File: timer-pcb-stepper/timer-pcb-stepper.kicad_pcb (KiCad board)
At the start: 4 copper layers, 75 x 72.5 mm, 30 parts, among them J1 JST_05, J10 JST_05, J11 Conn_01x04_Pin, J2 battery, J3 On/off, J4 JST_03, J5 JST_03, J6 JST_03, J7 JST_03, J8 JST_03_Led_panel, J9 JST_05, U2 ULN2003, U3 ULN2003, U4 ULN2003

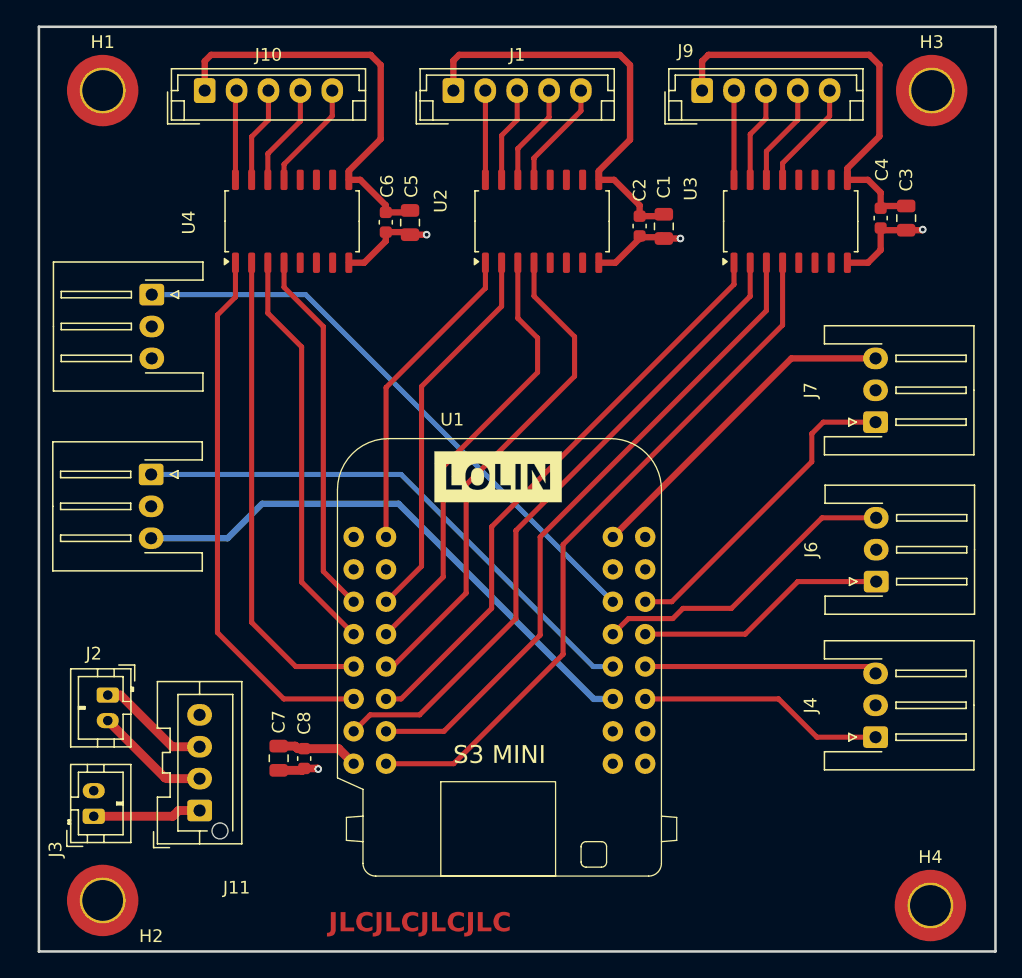
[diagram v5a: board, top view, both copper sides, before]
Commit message: ajout de text indicatif couche silkscreen sur les différents composants du PCB. ajout de test points sur 5V, GND, GPIO37 pour debugger et pin 15 (3.3V). connecteurs repositionés franc bord.
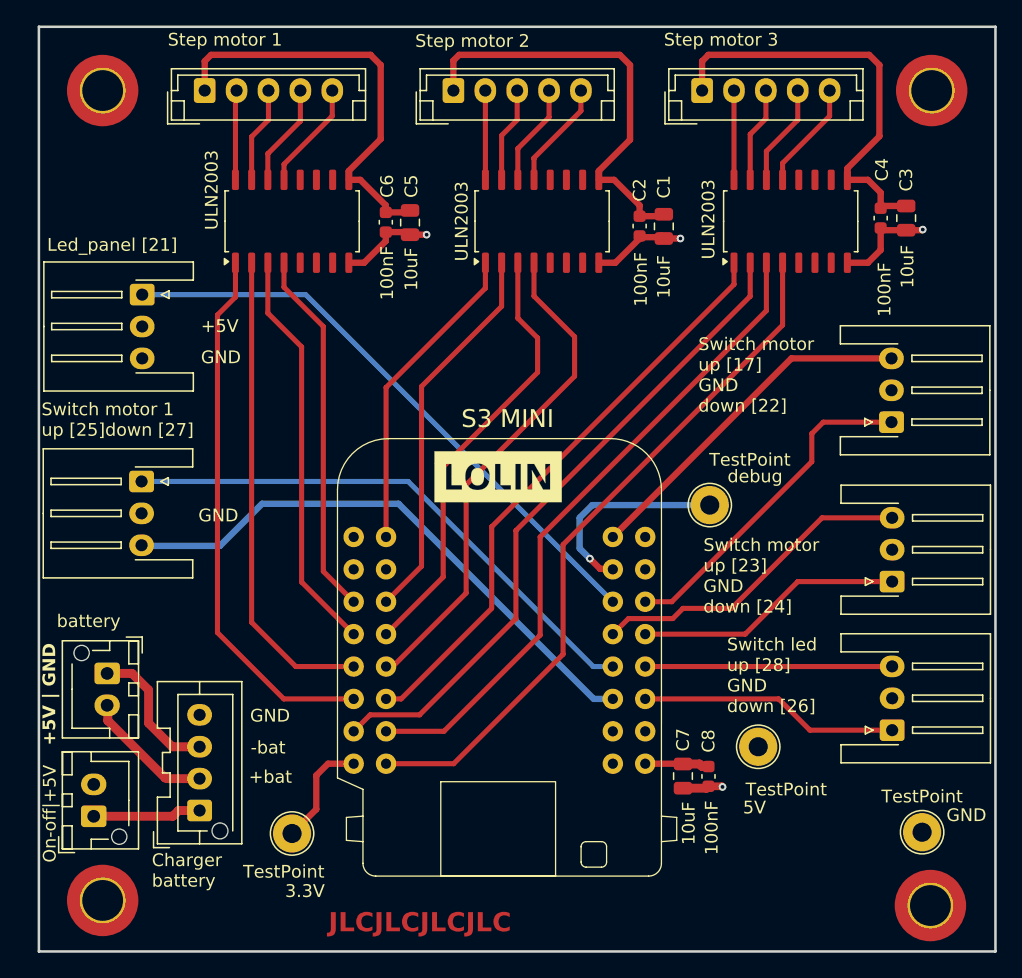
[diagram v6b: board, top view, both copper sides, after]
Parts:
- added TP1: TestPoint, TestPoint:TestPoint_Loop_D2.54mm_Drill1.5mm_Beaded, F.Cu at (69.8, 103.2)
- added TP2: TestPoint, TestPoint:TestPoint_Loop_D2.54mm_Drill1.5mm_Beaded, F.Cu at (106.4, 96.5)
- added TP3: TestPoint, TestPoint:TestPoint_Loop_D2.54mm_Drill1.5mm_Beaded, F.Cu at (102.6, 77.5)
- added TP4: TestPoint, TestPoint:TestPoint_Loop_D2.54mm_Drill1.5mm_Beaded, F.Cu at (119.2, 103.2)
- J2: footprint Connector_JST:JST_PH_B2B-PH-K_1x02_P2.00mm_Vertical -> Connector_JST:JST_XH_B2B-XH-AM_1x02_P2.50mm_Vertical
- J3: value On/off -> On-off|+5V; footprint Connector_JST:JST_PH_B2B-PH-K_1x02_P2.00mm_Vertical -> Connector_JST:JST_XH_B2B-XH-AM_1x02_P2.50mm_Vertical
- J8: value JST_03_Led_panel -> Led_panel [21]
- moved C7 31.7 mm to (100.5, 98.8)
- moved C8 31.7 mm to (102.5, 98.8)
- moved J2 1.70 mm to (55.4, 90.7)
- moved J4 1.41 mm to (116.9, 95.2)
- moved J6 1.25 mm to (116.9, 83.5)
- moved J7 1.25 mm to (116.8, 71.0)
- moved J5 0.93 mm to (58.0, 75.7)
- moved J8 0.75 mm to (58.1, 61.0)
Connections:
- U1 pad 15: +5V -> Net-(U1-3V)
- U1 pad 19: unconnected-(U1-GPIO37-Pad19) -> Net-(U1-GPIO37)
- U1 pad 32: unconnected-(U1-VBUS-Pad32) -> +5V
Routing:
- net Net-(U1-GPIO37): track 0.00 -> 16.3 mm, vias 0 -> 1
- net Net-(U1-3V): track 0.00 -> 8.65 mm
- net -BATT: track 8.88 -> 11.2 mm
- net Switch_Led_control_Up: track 19.3 -> 21.2 mm
- net +5V: track 106.0 -> 104.6 mm
- net Switch_motor_3_Down: track 25.2 -> 26.4 mm
- net Switch_motor_2_Up: track 24.4 -> 25.7 mm
- net Switch_motor_2_Down: track 19.8 -> 21.1 mm
- net +BATT: track 9.08 -> 10.3 mm
- net Switch_Led_control_Down: track 18.3 -> 19.4 mm
- net Switch_motor_1_Down: track 43.7 -> 44.7 mm
- net Switch_motor_3_Up: track 26.6 -> 27.6 mm
- net WS2812_Led: track 46.1 -> 46.9 mm
- net Switch_motor_1_Up: track 42.4 -> 43.0 mm
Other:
- board text added: "+5V"
- board text added: "+5V | GND"
- board text added: "+bat"
- board text added: "-bat"
- board text added: "3.3V"
- board text added: "5V"
- board text added: "Charger battery"
- board text added: "GND"
- board text added: "Step motor 1"
- board text added: "Step motor 2"
- board text added: "Step motor 3"
- board text added: "Switch led up [28] GND down [26]"
- board text added: "Switch motor 1 up [25]down [27]"
- board text added: "Switch motor up [17] GND down [22]"
- board text added: "Switch motor up [23] GND down [24]"
- board text added: "debug"

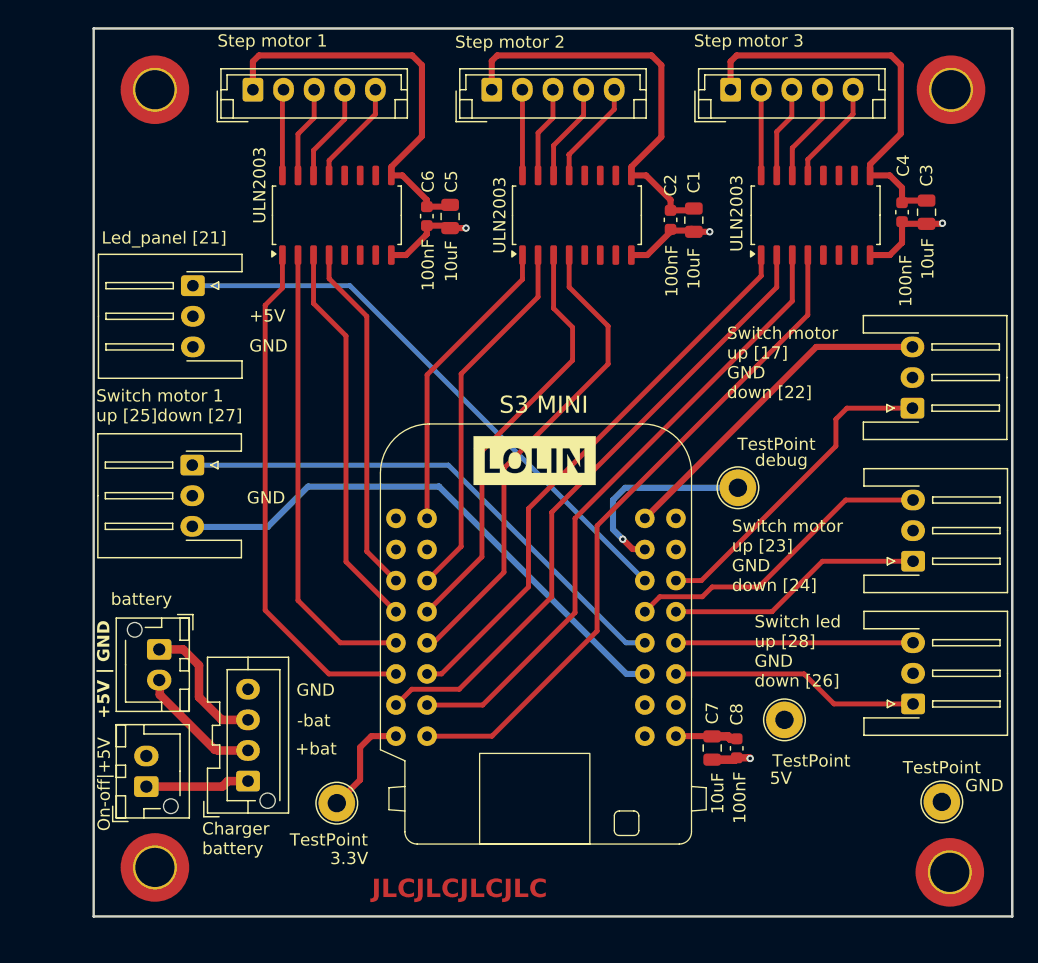
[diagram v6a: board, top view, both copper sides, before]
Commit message: mise à jour fichier blender pour impression 3D. Reste a mettre la bonne épaisseur pour le socle de la shell et percer les trous pour interrupteurs switch et on-off. déterminer ou placer entrées pour recharge et update code. comment fixer module recharge.
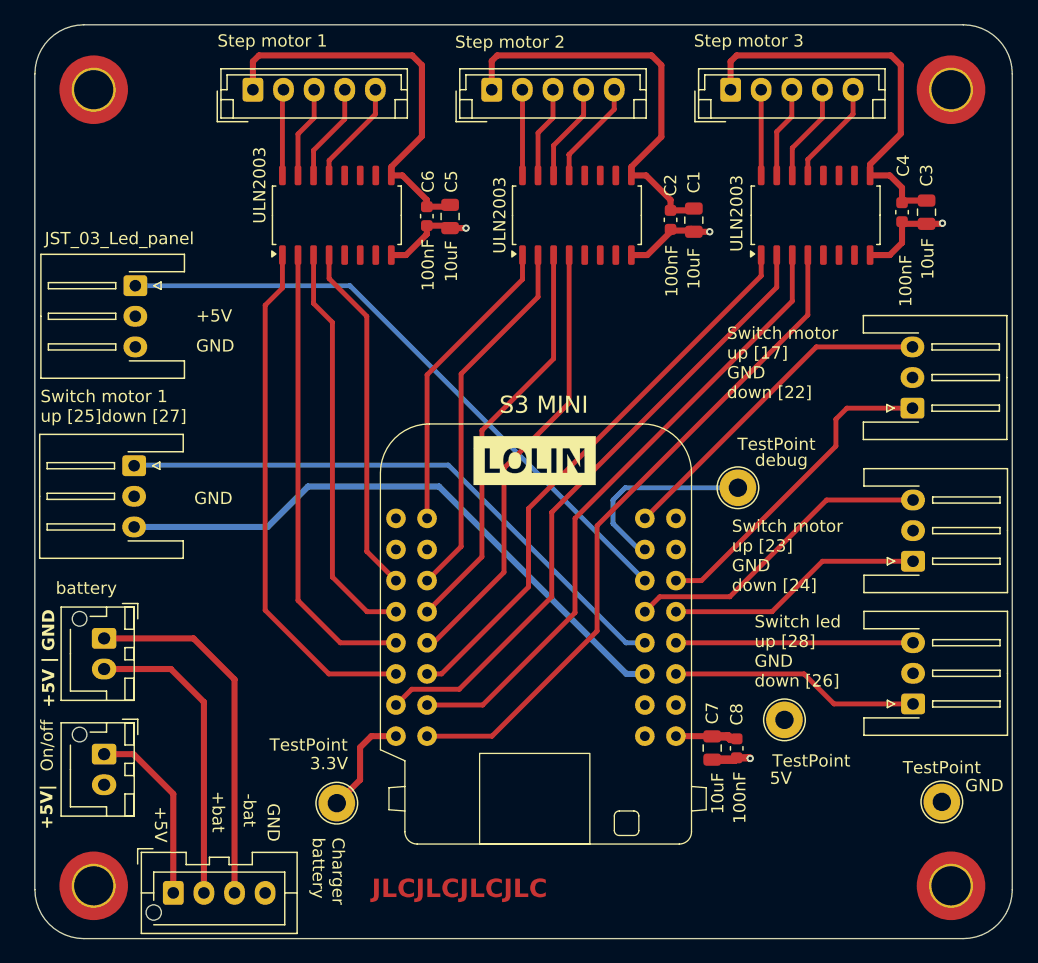
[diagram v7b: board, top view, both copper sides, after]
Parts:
- J3: value On-off|+5V -> On/off
- J8: value Led_panel [21] -> JST_03_Led_panel
- moved J11 11.0 mm to (56.5, 110.6), turned to 0 degrees
- moved H2 5.22 mm to (50.0, 110.0)
- moved H1 5.00 mm to (50.0, 45.0)
- moved J5 4.75 mm to (53.3, 75.7)
- moved J8 4.70 mm to (53.4, 61.0)
- moved J2 4.59 mm to (50.9, 89.8)
- moved J3 4.35 mm to (50.9, 99.2), turned to -90 degrees
- moved G*** 3.74 mm to (111.0, 107.0)
- moved G*** 2.37 mm to (88.9, 105.3)
- moved REF** 1.94 mm to (55.6, 51.7)
- moved H4 1.10 mm to (120.0, 110.0)
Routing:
- net -BATT: track 11.2 -> 29.5 mm
- net +BATT: track 10.3 -> 24.8 mm
- net On/off: track 8.49 -> 15.1 mm
- net Switch_motor_1_Up: track 43.0 -> 47.7 mm
- net Switch_motor_1_Down: track 44.7 -> 49.4 mm
- net WS2812_Led: track 46.9 -> 51.6 mm
- net M1D: track 39.4 -> 36.8 mm
- net M3C: track 31.9 -> 33.3 mm
- net M1C: track 34.7 -> 33.4 mm
- net Net-(U1-GPIO37): track 16.3 -> 16.1 mm, vias 1 -> 0
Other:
- board size 75 x 72.5 mm -> 79.8 x 74.6 mm
- board text added: "+5V|"
